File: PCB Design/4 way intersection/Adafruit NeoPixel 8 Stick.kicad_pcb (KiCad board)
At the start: 2 copper layers, 33 x 32.5 mm, 9 parts, among them CN1 1X4SMT, CN2 1X4SMT, CN3 1X4SMT, CN4 1X4SMT

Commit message: arrows
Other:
- board text removed: "DIN"
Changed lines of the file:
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@@
       (net 2 "GND") (pinfunction "4") (pintype "bidirectional") (solder_mask_margin 0.1016))
   )
+  (gr_line (start 139.192 107.95) (end 136.906 110.49) (layer "B.SilkS") (width 0.12))
+  (gr_line (start 148.844 106.426) (end 146.304 104.14) (layer "B.SilkS") (width 0.12))
+  (gr_line (start 148.844 106.426) (end 146.304 108.458) (layer "B.SilkS") (width 0.12))
+  (gr_line (start 130.048 106.426) (end 138.938 106.426) (layer "B.SilkS") (width 0.12))
+  (gr_line (start 138.938 106.426) (end 136.398 108.458) (layer "B.SilkS") (width 0.12))
+  (gr_line (start 139.192 107.95) (end 141.224 110.49) (layer "B.SilkS") (width 0.12))
+  (gr_line (start 139.192 96.266) (end 136.906 98.806) (layer "B.SilkS") (width 0.12))
+  (gr_line (start 139.192 105.156) (end 139.192 96.266) (layer "B.SilkS") (width 0.12))
+  (gr_line (start 139.192 116.84) (end 139.192 107.95) (layer "B.SilkS") (width 0.12))
+  (gr_line (start 138.938 106.426) (end 136.398 104.14) (layer "B.SilkS") (width 0.12))
+  (gr_line (start 139.192 96.266) (end 141.224 98.806) (layer "B.SilkS") (width 0.12))
+  (gr_line (start 139.954 106.426) (end 148.844 106.426) (layer "B.SilkS") (width 0.12))
   (gr_line (start 131.064 89.916) (end 146.812001 89.916) (layer "Edge.Cuts") (width 0.05))
   (gr_line (start 131.064 98.552) (end 131.064 89.916) (layer "Edge.Cuts") (width 0.05))
@@
   (gr_line (start 134.62 122.428) (end 131.064 122.428) (layer "Edge.Cuts") (width 0.05))
   (gr_line (start 146.812 98.552) (end 155.448 98.552) (layer "Edge.Cuts") (width 0.05))
-  (gr_text "4-7VDC" (at 139.192 116.586 90) (layer "B.SilkS")
-    (effects (font (size 1.143 1.143) (thickness 0.127)) (justify right top mirror))
-  )
-  (gr_text "DIN" (at 137.16 116.586 90) (layer "B.SilkS")
-    (effects (font (size 1.143 1.143) (thickness 0.127)) (justify right top mirror))
-  )
   (gr_text "4-7VDC" (at 152.654 131.4704 270) (layer "B.SilkS")
     (effects (font (size 1.143 1.143) (thickness 0.127)) (justify left bottom mirror))
-  )
-  (gr_text "DIN" (at 146.05 104.902) (layer "B.SilkS")
-    (effects (font (size 1.143 1.143) (thickness 0.127)) (justify right top mirror))
-  )
-  (gr_text "4-7VDC" (at 128.9812 107.0864) (layer "B.SilkS")
-    (effects (font (size 1.143 1.143) (thickness 0.127)) (justify right top mirror))
-  )
-  (gr_text "DIN" (at 137.414 99.822 90) (layer "B.SilkS")
-    (effects (font (size 1.143 1.143) (thickness 0.127)) (justify right top mirror))
   )
   (gr_text "DOUT" (at 155.194 131.4704 270) (layer "B.SilkS")
     (effects (font (size 1.143 1.143) (thickness 0.127)) (justify left bottom mirror))
   )
-  (gr_text "4-7VDC" (at 139.446 103.378 90) (layer "B.SilkS")
-    (effects (font (size 1.143 1.143) (thickness 0.127)) (justify right top mirror))
-  )
   (gr_text "GND" (at 150.622 131.4704 270) (layer "B.SilkS")
     (effects (font (size 1.143 1.143) (thickness 0.127)) (justify left bottom mirror))
-  )
-  (gr_text "DIN" (at 128.9812 105.0544) (layer "B.SilkS")
-    (effects (font (size 1.143 1.143) (thickness 0.127)) (justify right top mirror))
-  )
-  (gr_text "GND" (at 134.62 116.586 90) (layer "B.SilkS")
-    (effects (font (size 1.143 1.143) (thickness 0.127)) (justify right top mirror))
-  )
-  (gr_text "GND" (at 141.478 100.076 90) (layer "B.SilkS")
-    (effects (font (size 1.143 1.143) (thickness 0.127)) (justify right top mirror))
-  )
-  (gr_text "GND" (at 141.224 116.586 90) (layer "B.SilkS")
-    (effects (font (size 1.143 1.143) (thickness 0.127)) (justify right top mirror))
   )
   (gr_text "GND" (at 157.734 131.4704 270) (layer "B.SilkS")
     (effects (font (size 1.143 1.143) (thickness 0.127)) (justify left bottom mirror))
   )
-  (gr_text "GND" (at 128.9812 102.5144) (layer "B.SilkS")
-    (effects (font (size 1.143 1.143) (thickness 0.127)) (justify right top mirror))
-  )
-  (gr_text "4-7VDC" (at 142.24 106.934) (layer "B.SilkS")
-    (effects (font (size 1.143 1.143) (thickness 0.127)) (justify right top mirror))
-  )
-  (gr_text "GND" (at 145.542 102.362) (layer "B.SilkS")
-    (effects (font (size 1.143 1.143) (thickness 0.127)) (justify right top mirror))
-  )
-  (gr_text "GND" (at 145.542 108.966) (layer "B.SilkS")
-    (effects (font (size 1.143 1.143) (thickness 0.127)) (justify right top mirror))
-  )
-  (gr_text "GND" (at 134.874 99.822 90) (layer "B.SilkS")
-    (effects (font (size 1.143 1.143) (thickness 0.127)) (justify right top mirror))
-  )
-  (gr_text "GND" (at 128.9812 109.1184) (layer "B.SilkS")
-    (effects (font (size 1.143 1.143) (thickness 0.127)) (justify right top mirror))
-  )
   (segment (start 140.97 118.618) (end 141.3662 118.2218) (width 0.25) (layer "F.Cu") (net 1))

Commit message: 6 pin
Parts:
- moved D4 6.04 mm to (140.5, 119.9)
- moved D3 4.58 mm to (152.4, 108.0)
- moved CN1 4.16 mm to (154.2, 108.5)
- moved CN3 3.31 mm to (140.0, 121.7)
- moved D5 2.96 mm to (140.7, 96.3)
- moved CN4 2.81 mm to (141.2, 94.2)
- moved D2 2.16 mm to (140.7, 108.0)
- moved D1 1.98 mm to (128.8, 108.0)
- moved CN2 0.52 mm to (126.9, 107.4)
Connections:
- CN1 pad 1: GND -> Net-(CN1-Pad1)
- CN1 pad 3: +5V -> GND
- CN1 pad 4: GND -> Net-(D3-Pad2)
- CN4 pad 1: GND -> Net-(CN1-Pad1)
- CN4 pad 2: Net-(CN4-Pad2) -> Net-(CN1-Pad2)
- CN4 pad 3: +5V -> GND
- CN4 pad 4: GND -> Net-(CN4-Pad4)
- D3 pad 2: Net-(CN1-Pad2) -> Net-(D3-Pad2)
- D5 pad 2: Net-(CN4-Pad2) -> Net-(CN4-Pad4)
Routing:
- net Net-(CN1-Pad1): track 0.00 -> 57.4 mm, vias 0 -> 2
- net Net-(CN1-Pad2): track 0.00 -> 57.3 mm, vias 1 -> 2
- net +5V: track 52.7 -> 73.8 mm
- net Net-(D4-Pad2): track 11.5 -> 20.2 mm, vias 2 -> 0
- net Net-(CN3-Pad3): track 4.15 -> 0.00 mm
- net Net-(CN2-Pad3): track 4.05 -> 0.00 mm
- net Net-(D3-Pad2): track 0.00 -> 3.79 mm, vias 0 -> 1
- net Net-(CN4-Pad4): track 0.00 -> 3.79 mm, vias 0 -> 1
- net Net-(D2-Pad2): track 5.32 -> 8.11 mm
- net Net-(D1-Pad2): track 5.57 -> 8.36 mm
- net GND: track 0.00 -> 2.17 mm
- net Net-(CN4-Pad2): vias 1 -> 0
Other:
- board size 33 x 32.5 mm -> 36.2 x 36.2 mm
- board text removed: "4-7VDC"
- board text removed: "DOUT"
- board text removed: "GND"

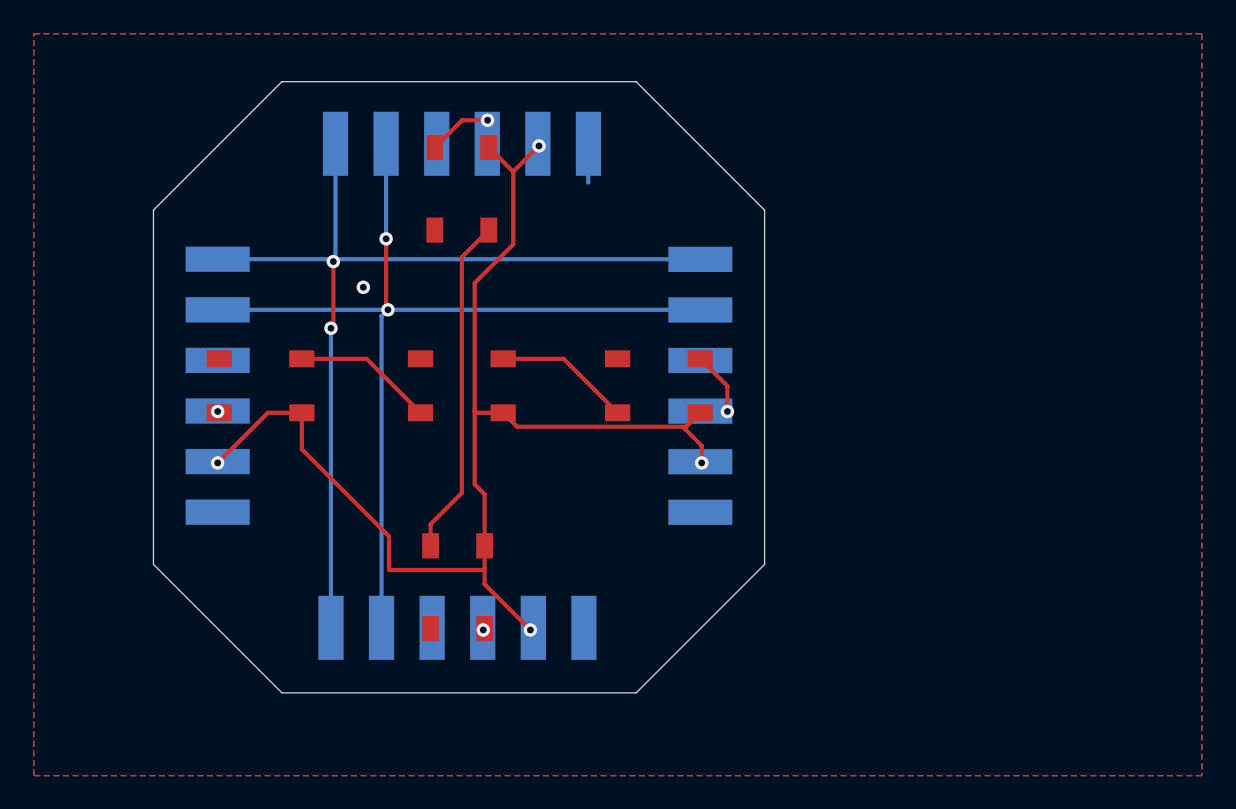
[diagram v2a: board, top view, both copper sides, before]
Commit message: move vias off pads
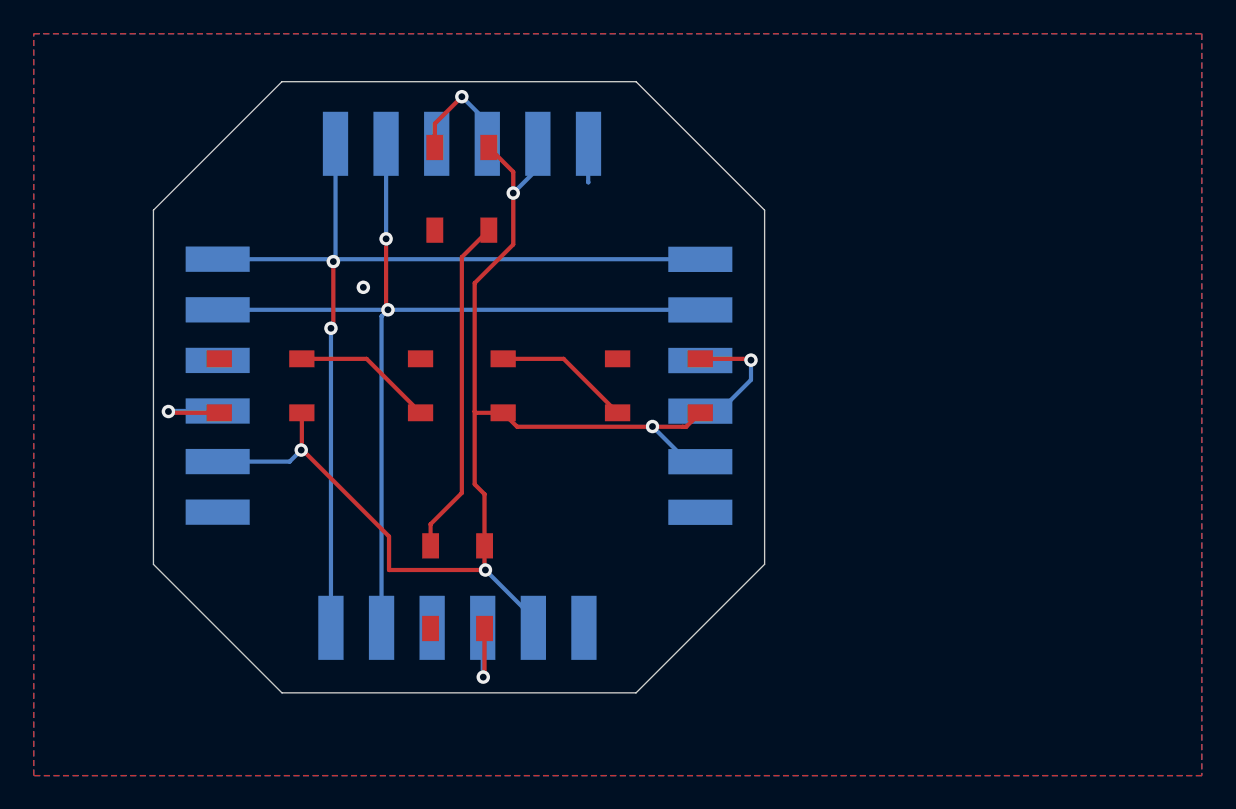
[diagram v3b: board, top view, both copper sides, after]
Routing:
- net Net-(CN2-Pad3): track 0.00 -> 5.98 mm
- net Net-(CN3-Pad3): track 0.00 -> 5.85 mm
- net Net-(D3-Pad2): track 3.79 -> 7.98 mm
- net Net-(CN4-Pad4): track 3.79 -> 7.09 mm
- net +5V: track 73.8 -> 75.1 mm
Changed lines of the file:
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@@
   (gr_line (start 130.048 89.916) (end 122.428 97.536) (layer "Edge.Cuts") (width 0.05))
   (gr_line (start 151.048 89.916) (end 158.667999 97.536) (layer "Edge.Cuts") (width 0.05))
-  (segment (start 143.764 95.264) (end 143.764 95.25) (width 0.25) (layer "F.Cu") (net 1))
   (segment (start 136.398 116.8804) (end 136.398 118.872) (width 0.25) (layer "F.Cu") (net 1))
   (segment (start 143.764 95.264) (end 142.316 93.816) (width 0.25) (layer "F.Cu") (net 1))
@@
   (segment (start 131.228 109.55) (end 131.228 111.7104) (width 0.25) (layer "F.Cu") (net 1))
   (segment (start 141.986 118.872) (end 142.062 118.796) (width 0.25) (layer "F.Cu") (net 1))
-  (segment (start 142.062 119.71) (end 142.062 118.796) (width 0.25) (layer "F.Cu") (net 1))
   (segment (start 143.9942 110.3782) (end 153.8122 110.3782) (width 0.25) (layer "F.Cu") (net 1))
   (segment (start 131.228 111.7104) (end 136.398 116.8804) (width 0.25) (layer "F.Cu") (net 1))
@@
   (segment (start 142.062 117.438) (end 142.062 114.376) (width 0.25) (layer "F.Cu") (net 1))
   (segment (start 143.166 109.55) (end 143.9942 110.3782) (width 0.25) (layer "F.Cu") (net 1))
-  (segment (start 154.94 112.522) (end 154.94 111.506) (width 0.25) (layer "F.Cu") (net 1))
   (segment (start 141.478 109.474) (end 141.478 101.854) (width 0.25) (layer "F.Cu") (net 1))
-  (segment (start 143.764 95.25) (end 145.288 93.726) (width 0.25) (layer "F.Cu") (net 1))
-  (segment (start 126.238 112.522) (end 129.21 109.55) (width 0.25) (layer "F.Cu") (net 1))
-  (segment (start 154.94 111.506) (end 153.8122 110.3782) (width 0.25) (layer "F.Cu") (net 1))
   (segment (start 141.478 101.854) (end 143.764 99.568) (width 0.25) (layer "F.Cu") (net 1))
   (segment (start 141.478 109.474) (end 141.554 109.55) (width 0.25) (layer "F.Cu") (net 1))
@@
   (segment (start 136.398 118.872) (end 141.986 118.872) (width 0.25) (layer "F.Cu") (net 1))
   (segment (start 153.8122 110.3782) (end 154.0218 110.3782) (width 0.25) (layer "F.Cu") (net 1))
-  (segment (start 129.21 109.55) (end 131.228 109.55) (width 0.25) (layer "F.Cu") (net 1))
   (segment (start 142.062 118.796) (end 142.062 117.438) (width 0.25) (layer "F.Cu") (net 1))
   (segment (start 143.764 99.568) (end 143.764 95.264) (width 0.25) (layer "F.Cu") (net 1))
   (segment (start 142.062 114.376) (end 141.478 113.792) (width 0.25) (layer "F.Cu") (net 1))
-  (segment (start 144.78 122.428) (end 142.062 119.71) (width 0.25) (layer "F.Cu") (net 1))
-  (via (at 144.78 122.428) (size 0.8) (drill 0.4) (layers "F.Cu" "B.Cu") (net 1))
-  (via (at 145.288 93.726) (size 0.8) (drill 0.4) (layers "F.Cu" "B.Cu") (net 1))
-  (via (at 154.94 112.522) (size 0.8) (drill 0.4) (layers "F.Cu" "B.Cu") (net 1))
-  (via (at 126.238 112.522) (size 0.8) (drill 0.4) (layers "F.Cu" "B.Cu") (net 1))
+  (via (at 142.113 118.872) (size 0.8) (drill 0.4) (layers "F.Cu" "B.Cu") (net 1))
+  (via (at 143.764 96.52) (size 0.8) (drill 0.4) (layers "F.Cu" "B.Cu") (net 1))
+  (via (at 152.019 110.363) (size 0.8) (drill 0.4) (layers "F.Cu" "B.Cu") (net 1))
+  (via (at 131.191 111.76) (size 0.8) (drill 0.4) (layers "F.Cu" "B.Cu") (net 1))
+  (segment (start 126.238 112.442) (end 130.509 112.442) (width 0.25) (layer "B.Cu") (net 1))
+  (segment (start 154.857999 112.45) (end 154.106 112.45) (width 0.25) (layer "B.Cu") (net 1))
+  (segment (start 154.106 112.45) (end 152.019 110.363) (width 0.25) (layer "B.Cu") (net 1))
+  (segment (start 145.224 93.599) (end 145.224 95.06) (width 0.25) (layer "B.Cu") (net 1))
+  (segment (start 145.224 95.06) (end 143.764 96.52) (width 0.25) (layer "B.Cu") (net 1))
+  (segment (start 144.954 122.301) (end 144.954 121.713) (width 0.25) (layer "B.Cu") (net 1))
+  (segment (start 130.509 112.442) (end 131.191 111.76) (width 0.25) (layer "B.Cu") (net 1))
+  (segment (start 144.954 121.713) (end 142.113 118.872) (width 0.25) (layer "B.Cu") (net 1))
   (via (at 134.874 102.108) (size 0.8) (drill 0.4) (layers "F.Cu" "B.Cu") (free) (net 2))
   (segment (start 148.208 93.726) (end 148.208 95.876) (width 0.25) (layer "B.Cu") (net 2))
@@
   (segment (start 136.224 93.599) (end 136.224 99.234) (width 0.25) (layer "B.Cu") (net 3))
   (segment (start 126.238 103.442) (end 136.334 103.442) (width 0.25) (layer "B.Cu") (net 3))
-  (via (at 126.238 109.474) (size 0.8) (drill 0.4) (layers "F.Cu" "B.Cu") (net 4))
+  (segment (start 123.393 109.55) (end 126.328 109.55) (width 0.25) (layer "F.Cu") (net 4))
+  (segment (start 123.317 109.474) (end 123.393 109.55) (width 0.25) (layer "F.Cu") (net 4))
+  (via (at 123.317 109.474) (size 0.8) (drill 0.4) (layers "F.Cu" "B.Cu") (net 4))
+  (segment (start 123.349 109.442) (end 123.317 109.474) (width 0.25) (layer "B.Cu") (net 4))
+  (segment (start 126.238 109.442) (end 123.349 109.442) (width 0.25) (layer "B.Cu") (net 4))
   (segment (start 135.066 106.35) (end 138.266 109.55) (width 0.25) (layer "F.Cu") (net 5))
   (segment (start 131.228 106.35) (end 135.066 106.35) (width 0.25) (layer "F.Cu") (net 5))
   (segment (start 143.166 106.35) (end 146.75 106.35) (width 0.25) (layer "F.Cu") (net 6))
   (segment (start 146.75 106.35) (end 149.95 109.55) (width 0.25) (layer "F.Cu") (net 6))
-  (segment (start 154.85 106.35) (end 156.464 107.964) (width 0.25) (layer "F.Cu") (net 7))
-  (segment (start 156.464 107.964) (end 156.464 109.474) (width 0.25) (layer "F.Cu") (net 7))
-  (via (at 156.464 109.474) (size 0.8) (drill 0.4) (layers "F.Cu" "B.Cu") (net 7))
+  (segment (start 157.785 106.35) (end 157.861 106.426) (width 0.25) (layer "F.Cu") (net 7))
+  (segment (start 154.85 106.35) (end 157.785 106.35) (width 0.25) (layer "F.Cu") (net 7))
+  (via (at 157.861 106.426) (size 0.8) (drill 0.4) (layers "F.Cu" "B.Cu") (net 7))
+  (segment (start 154.857999 109.45) (end 156.007999 109.45) (width 0.25) (layer "B.Cu") (net 7))
+  (segment (start 156.007999 109.45) (end 157.861 107.596999) (width 0.25) (layer "B.Cu") (net 7))
+  (segment (start 157.861 107.596999) (end 157.861 106.426) (width 0.25) (layer "B.Cu") (net 7))
   (segment (start 138.862 117.438) (end 138.862 116.154) (width 0.25) (layer "F.Cu") (net 8))
   (segment (start 138.862 116.154) (end 140.716 114.3) (width 0.25) (layer "F.Cu") (net 8))
   (segment (start 140.716 114.3) (end 140.716 100.316) (width 0.25) (layer "F.Cu") (net 8))
   (segment (start 140.716 100.316) (end 142.316 98.716) (width 0.25) (layer "F.Cu") (net 8))
-  (via (at 141.986 122.428) (size 0.8) (drill 0.4) (layers "F.Cu" "B.Cu") (net 9))
-  (segment (start 139.116 93.816) (end 140.73 92.202) (width 0.25) (layer "F.Cu") (net 10))
-  (segment (start 140.73 92.202) (end 142.24 92.202) (width 0.25) (layer "F.Cu") (net 10))
-  (via (at 142.24 92.202) (size 0.8) (drill 0.4) (layers "F.Cu" "B.Cu") (net 10))
+  (segment (start 141.986 125.222) (end 142.062 125.146) (width 0.25) (layer "F.Cu") (net 9))
+  (segment (start 142.062 125.146) (end 142.062 122.338) (width 0.25) (layer "F.Cu") (net 9))
+  (via (at 141.986 125.222) (size 0.8) (drill 0.4) (layers "F.Cu" "B.Cu") (net 9))
+  (segment (start 141.954 122.301) (end 141.954 125.19) (width 0.25) (layer "B.Cu") (net 9))
+  (segment (start 141.954 125.19) (end 141.986 125.222) (width 0.25) (layer "B.Cu") (net 9))
+  (segment (start 139.116 92.405) (end 140.716 90.805) (width 0.25) (layer "F.Cu") (net 10))
+  (segment (start 139.116 93.816) (end 139.116 92.405) (width 0.25) (layer "F.Cu") (net 10))
+  (via (at 140.716 90.805) (size 0.8) (drill 0.4) (layers "F.Cu" "B.Cu") (net 10))
+  (segment (start 142.224 92.313) (end 142.224 93.599) (width 0.25) (layer "B.Cu") (net 10))
+  (segment (start 140.716 90.805) (end 142.224 92.313) (width 0.25) (layer "B.Cu") (net 10))
   (segment (start 132.954 104.536) (end 133.096 104.394) (width 0.25) (layer "F.Cu") (net 11))
   (segment (start 133.096 104.394) (end 133.096 100.584) (width 0.25) (layer "F.Cu") (net 11))
